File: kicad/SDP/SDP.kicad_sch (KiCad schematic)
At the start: 29 parts

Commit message: Added sheet
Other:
- added sheet GrinderSubsystem (grindersubsystem.kicad_sch)
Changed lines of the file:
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@@
     (pin "2")
-  )
-  (symbol (lib_id "power:+24V") (at 39.37 31.75 0) (unit 1)
-    (in_bom yes) (on_board yes) (fields_autoplaced)
-    (property "Reference" "#PWR?" (id 0) (at 39.37 35.56 0)
-      (effects (font (size 1.27 1.27)) hide)
-    )
-    (property "Value" "+24V" (id 1) (at 39.37 26.67 0))
-    (property "Footprint" "" (id 2) (at 39.37 31.75 0)
-      (effects (font (size 1.27 1.27)) hide)
-    )
-    (property "Datasheet" "" (id 3) (at 39.37 31.75 0)
-      (effects (font (size 1.27 1.27)) hide)
-    )
-    (pin "1")
   )
   (symbol (lib_id "Device:C") (at 666.75 21.59 0) (unit 1)
@@
     (pin "1")
   )
+  (symbol (lib_id "power:+12V") (at 39.37 33.02 0) (unit 1)
+    (in_bom yes) (on_board yes) (fields_autoplaced)
+    (property "Reference" "#PWR?" (id 0) (at 39.37 36.83 0)
+      (effects (font (size 1.27 1.27)) hide)
+    )
+    (property "Value" "+12V" (id 1) (at 39.37 27.94 0))
+    (property "Footprint" "" (id 2) (at 39.37 33.02 0)
+      (effects (font (size 1.27 1.27)) hide)
+    )
+    (property "Datasheet" "" (id 3) (at 39.37 33.02 0)
+      (effects (font (size 1.27 1.27)) hide)
+    )
+    (pin "1")
+  )
   (symbol (lib_name "GND_2") (lib_id "power:GND") (at 226.06 223.52 0) (unit 1)
     (in_bom yes) (on_board yes) (fields_autoplaced)
@@
     (pin "1")
   )
-  (sheet (at 326.39 33.02) (size 22.86 19.05) (fields_autoplaced)
+  (sheet (at 356.87 60.96) (size 20.32 19.05) (fields_autoplaced)
     (stroke (width 0.1524) (type solid) (color 0 0 0 0))
     (fill (color 0 0 0 0.0000))
-    (property "Sheet name" "FilterSubsystem" (id 0) (at 326.39 32.3084 0)
+    (property "Sheet name" "GrinderSubsystem" (id 0) (at 356.87 60.2484 0)
       (effects (font (size 1.27 1.27)) (justify left bottom))
     )
-    (property "Sheet file" "filtersubsystem.kicad_sch" (id 1) (at 326.39 52.6546 0)
+    (property "Sheet file" "grindersubsystem.kicad_sch" (id 1) (at 356.87 80.5946 0)
+      (effects (font (size 1.27 1.27)) (justify left top))
+    )
+  )
+  (sheet (at 356.87 31.75) (size 20.32 19.05) (fields_autoplaced)
+    (stroke (width 0.1524) (type solid) (color 0 0 0 0))
+    (fill (color 0 0 0 0.0000))
+    (property "Sheet name" "FilterSubsystem" (id 0) (at 356.87 31.0384 0)
+      (effects (font (size 1.27 1.27)) (justify left bottom))
+    )
+    (property "Sheet file" "filtersubsystem.kicad_sch" (id 1) (at 356.87 51.3846 0)
       (effects (font (size 1.27 1.27)) (justify left top))
     )
@@
     (path "/" (page "1"))
     (path "/a4a83c44-c8e0-453d-a09d-7474e32229cb" (page "2"))
+    (path "/60ab11df-7ec6-4862-a63f-21a5fb7314af" (page "3"))
   )
   (symbol_instances
@@
       (reference "#PWR?") (unit 1) (value "+3.3V") (footprint "")
     )
-    (path "/a4a83c44-c8e0-453d-a09d-7474e32229cb/101b1325-4279-4b67-96d2-6b5c97b1c400"
-      (reference "#PWR?") (unit 1) (value "+24V") (footprint "")
-    )
     (path "/13d8bfa6-d7d2-43b6-8fd6-aa77f4d342d5"
       (reference "#PWR?") (unit 1) (value "GND") (footprint "")
-    )
-    (path "/1be3e15d-4b9c-4cb1-b64b-2e6c6e28a3d9"
-      (reference "#PWR?") (unit 1) (value "+24V") (footprint "")
     )
     (path "/a4a83c44-c8e0-453d-a09d-7474e32229cb/22bb47d2-cad7-4e6f-9d0c-9f1abf96059d"
@@
       (reference "#PWR?") (unit 1) (value "GND") (footprint "")
     )
+    (path "/a4a83c44-c8e0-453d-a09d-7474e32229cb/c3b10306-ffea-4360-a540-14b7f64a3a06"
+      (reference "#PWR?") (unit 1) (value "+12V") (footprint "")
+    )
     (path "/c7457898-24d2-471b-adfd-6c8f1092010b"
       (reference "#PWR?") (unit 1) (value "+3.3VA") (footprint "")
@@
       (reference "#PWR?") (unit 1) (value "+3.3V") (footprint "")
     )
+    (path "/e3807980-a1cd-416c-873b-dd543df8b2fd"
+      (reference "#PWR?") (unit 1) (value "+12V") (footprint "")
+    )
     (path "/e4860a43-b5c8-40dc-8cba-8d3d99207cb6"

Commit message: Updated schematics
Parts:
- removed J?: Conn_01x06, symbol Connector_Generic:Conn_01x06
- added J?: RJ25, symbol Connector:RJ25
- added R?: 50k, symbol Device:R_Small
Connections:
- net +3V3: now also J?.2, R?.2
- net GND: now also J?.3
- net P13_MCLR: now also J?.1, R?.1
- net P26_PGC: now also J?.5
- net P27_PGD: now also J?.4
- net P6_GRD_RLY: now reaches U?.6 (T2CK/RC1)
- net P7_HTR_RLY: now reaches U?.7 (T3CK/RC2)
- no-connect marks 59 -> 60
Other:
- added sheet WaterSubsystem (watersubsystem.kicad_sch)

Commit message: Updated schematics
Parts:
- removed C? (x6): 0.1uF, symbol Device:C
- removed C?: 10uF, symbol Device:C
- removed U?: PIC24FJ128GA010-I_PT, TQFP100_12x12MC_MCH, symbol SDP-rescue:PIC24FJ128GA010-I_PT-2021-11-26_22-35-22
- added J?: Conn_01x04, symbol Connector_Generic:Conn_01x04
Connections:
- net +3V3: now also J?.3 (Pin_3)
- net GND: now also J?.4 (Pin_4)
- net P56_SDA1: now reaches U?.56 (SDA1/RG3)
- net P56_SDA1: now also J?.2 (Pin_2)
- net P57_SCL1: now reaches U?.57 (SCL1/RG2)
- net P57_SCL1: now also J?.1 (Pin_1)
- net P58_SCL2: now reaches U?.58 (SCL2/RA2)
- net P76_EN: now reaches U?.76 (OC2/RD1)
- net P77_STEP: now reaches U?.77 (OC3/RD2)
- net P78_DIR: now reaches U?.78 (PMBE/OC4/RD3)
- net P79_EN: now reaches U?.79 (IC5/RD12)
- net P80_STEP: now reaches U?.80 (CN19/RD13)
- net P81_DIR: now reaches U?.81 (PMWR/OC5/CN13/RD4)
- net P82_EN: now reaches U?.82 (PMRD/CN14/RD5)
- net P83_STEP: now reaches U?.83 (CN15/RD6)
- net P84_DIR: now reaches U?.84 (CN16/RD7)
- net P87_MTR1: now reaches U?.87 (RF0)
- net P88_MTR2: now reaches U?.88 (RF1)
- net P91_TEMP: now reaches U?.91 (RA6)
- net P95_TOF1_CE: now reaches U?.95 (RG14)
- net P96_TOF2_CE: now reaches U?.96 (RG12)
- net P97_TOF3_CE: now reaches U?.97 (RG13)
- net P59_!EN renamed P59_SDA2
- net P89_STEP: no longer names the net of U?.89 (RG1)
- net P90_DIR: no longer names the net of U?.90 (RG0)
- no-connect marks 60 -> 1
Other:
- added sheet BrewingSubsystem (brewingsubsystem.kicad_sch)
- note added: "LCD"
- note removed: "Bluetooth UART"
- note removed: "I2C Pins"
- note removed: "MPN: PIC24FJ128GA010-I_TP"

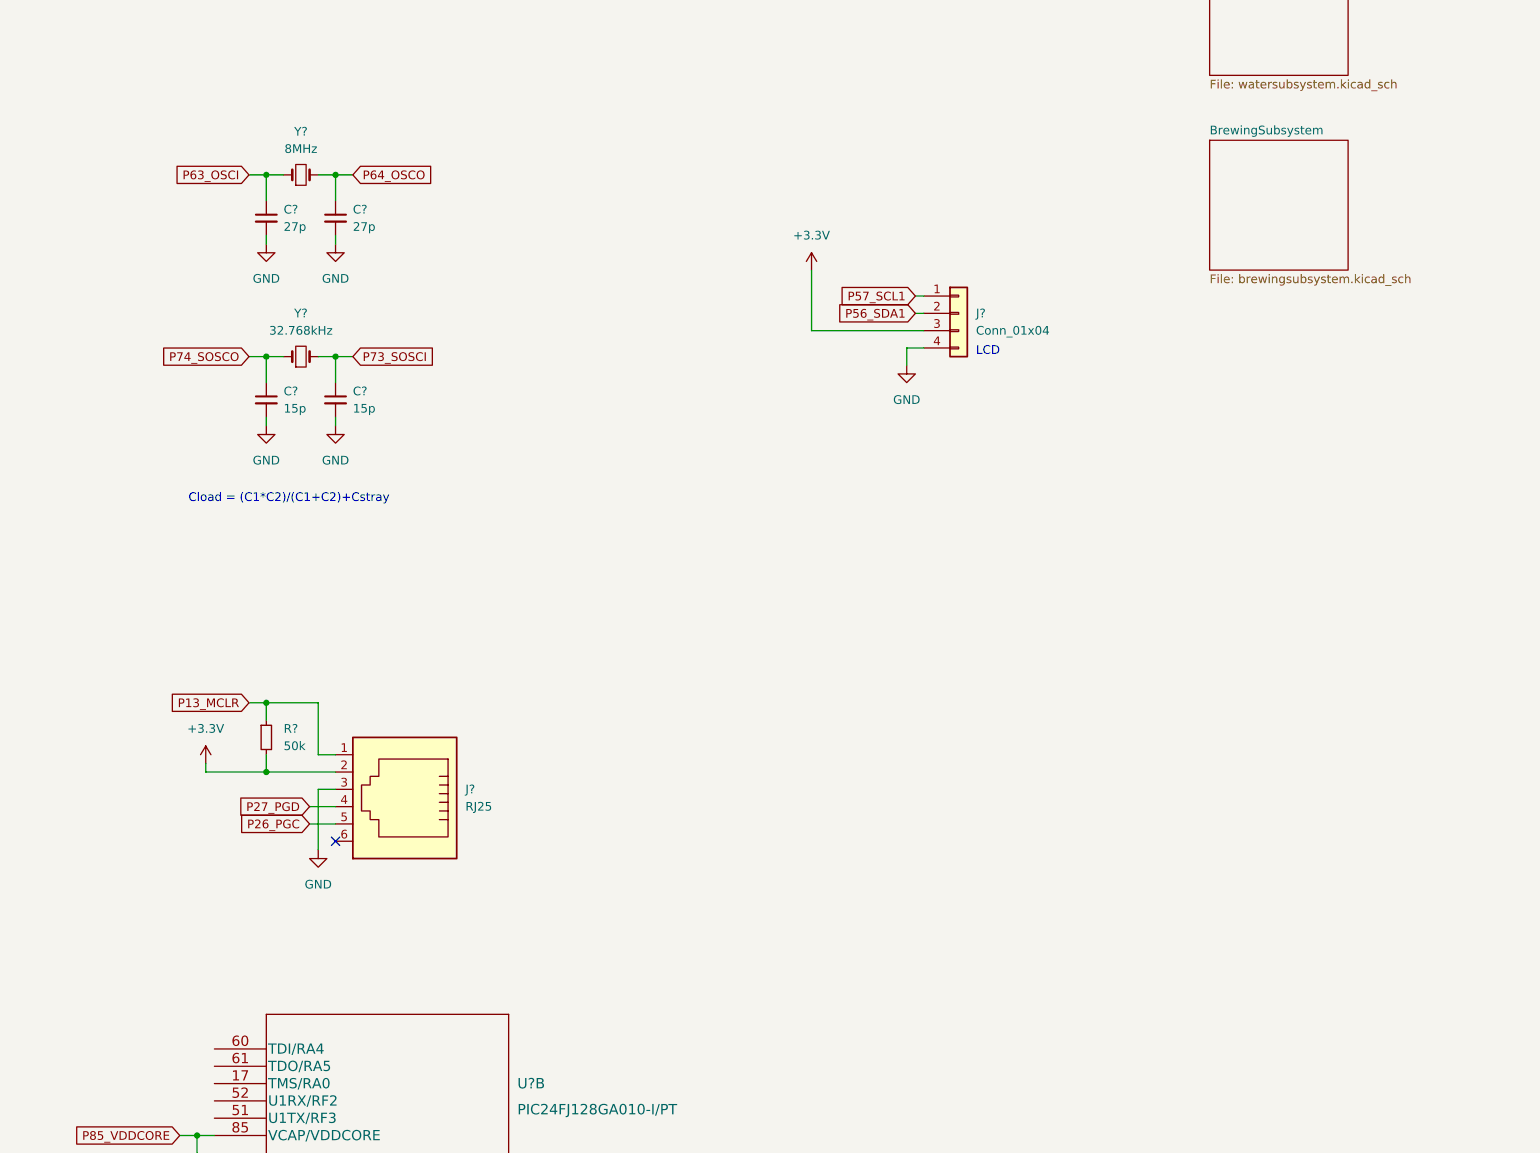
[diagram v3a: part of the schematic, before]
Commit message: Added DS3231 RTC and HM-10 BLE module
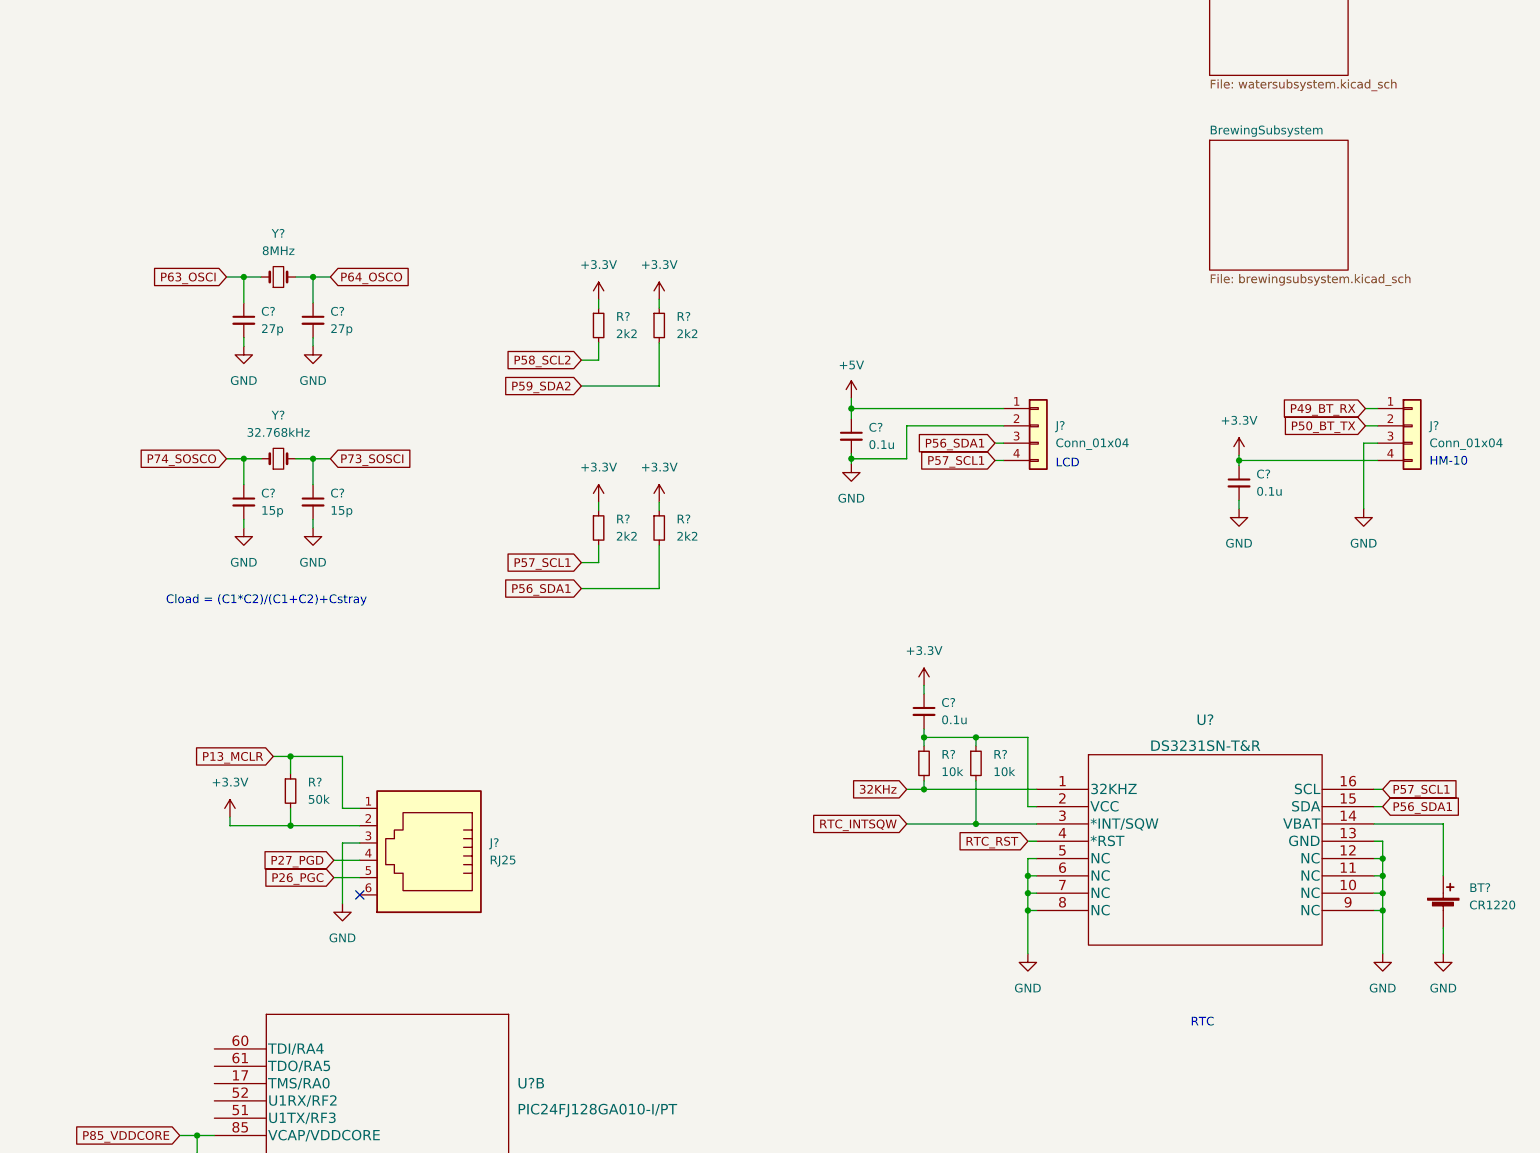
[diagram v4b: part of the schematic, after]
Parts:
- added BT?: CR1220, symbol Device:Battery_Cell
- added C? (x3): 0.1u, symbol Device:C_Small
- added J?: Conn_01x04, symbol Connector_Generic:Conn_01x04
- added R? (x2): 10k, symbol Device:R_Small
- added R? (x4): 2k2, symbol Device:R_Small
- added U?: DS3231SN-T&R, 21-0042B_16_MXM, symbol 2022-02-03_02-37-37:DS3231SN-T&R
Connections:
- net +3V3: now also C?.1, C?.1, J?.4 (Pin_4), R?.1, R?.1, R?.1, R?.1; no longer J?.3 (Pin_3)
- net +5V: now also J?.1 (Pin_1), C?.1
- net GND: now also J?.2 (Pin_2), BT?.2 (-), C?.2, C?.2, J?.3 (Pin_3), U?.10 (NC), U?.11 (NC), U?.12 (NC), U?.13 (GND), U?.5 (NC), U?.6 (NC), U?.7 (NC), U?.8 (NC), U?.9 (NC); no longer J?.4 (Pin_4)
- net P49_BT_RX: now also J?.1 (Pin_1)
- net P50_BT_TX: now also J?.2 (Pin_2)
- net P56_SDA1: now also J?.3 (Pin_3), R?.2, U?.15 (SDA); no longer J?.2 (Pin_2)
- net P57_SCL1: now also J?.4 (Pin_4), R?.2, U?.16 (SCL); no longer J?.1 (Pin_1)
- net P58_SCL2: now also R?.2
- net P59_SDA2: now also R?.2
- new net: BT?.1 (+), U?.14 (VBAT)
- new net: C?.2, R?.1, R?.1, U?.2 (VCC)
- new net 32KHz: R?.2, U?.1 (32KHZ)
- new net RTC_INTSQW: R?.2, U?.3 (*INT/SQW)
- new net RTC_RST: U?.4 (*RST)
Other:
- note added: "HM-10"
- note added: "RTC"
- moved on the sheet: C?, J?, R?, Y?

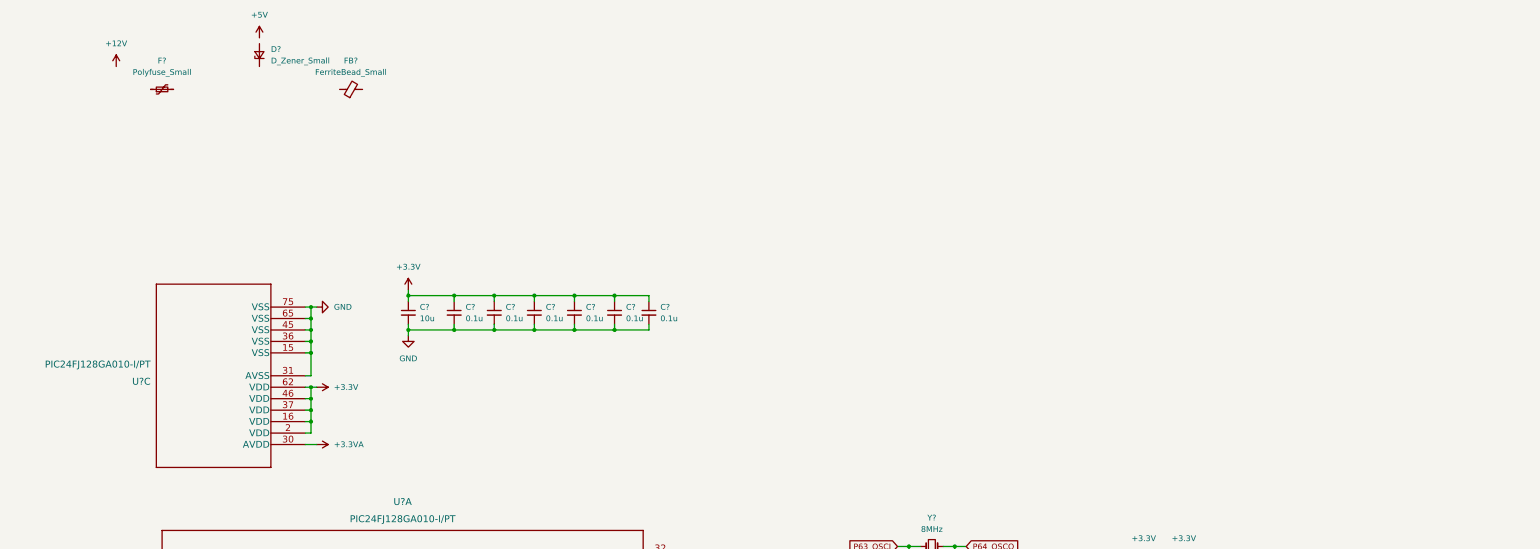
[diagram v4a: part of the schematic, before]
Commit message: Added 5V and 3.3V voltage regulators
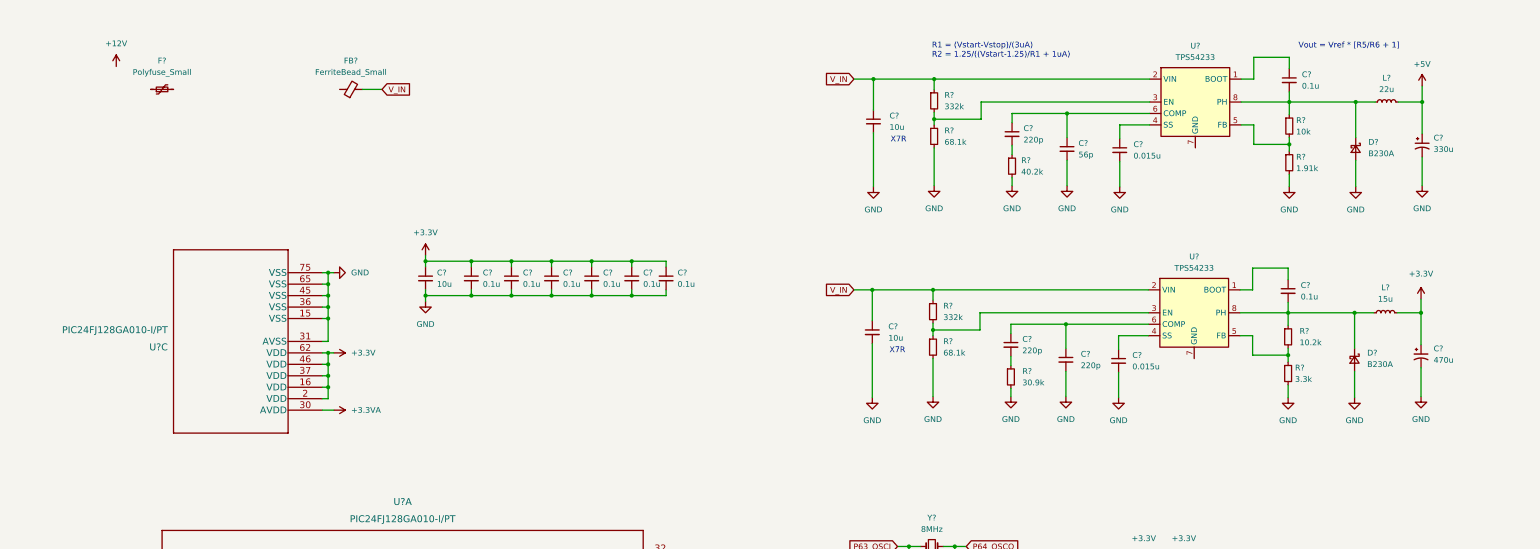
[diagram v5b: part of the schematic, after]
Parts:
- removed D?: D_Zener_Small, symbol Device:D_Zener_Small
- added C? (x3): 220p, symbol Device:C_Small
- added C? (x2): 10u, symbol Device:C_Small
- added C? (x2): 0.015u, symbol Device:C_Small
- added C?: 56p, symbol Device:C_Small
- added C?: 470u, symbol Device:C_Polarized_Small_US
- added C? (x2): 0.1u, symbol Device:C_Small
- added C?: 330u, symbol Device:C_Polarized_Small_US
- added D? (x2): B230A, symbol Device:D_Schottky_Small
- added L?: 22u, symbol Device:L_Small
- added L?: 15u, symbol Device:L_Small
- added R? (x2): 68.1k, symbol Device:R_Small
- added R?: 10.2k, symbol Device:R_Small
- added R?: 10k, symbol Device:R_Small
- added R?: 30.9k, symbol Device:R_Small
- added R? (x2): 332k, symbol Device:R_Small
- added R?: 1.91k, symbol Device:R_Small
- added R?: 3.3k, symbol Device:R_Small
- added R?: 40.2k, symbol Device:R_Small
- added U? (x2): TPS54233, Package_SO:SOIC-8_3.9x4.9mm_P1.27mm, symbol Regulator_Switching:TPS54233
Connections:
- net +3V3: now also C?.1, L?.2
- net +5V: now also C?.1, L?.2
- net GND: now also C?.2, C?.2, C?.2, C?.2, C?.2, C?.2, C?.2, C?.2, D?.2 (A), D?.2 (A), R?.2, R?.2, R?.2, R?.2, R?.2, R?.2
- net V_IN: now reaches FB?.2
- net V_IN: now also C?.1, C?.1, R?.1, R?.1, U?.2 (VIN), U?.2 (VIN)
- new net: C?.1, C?.1, U?.6 (COMP) (x2)
- new net: C?.1, U?.4 (SS) (x2)
- new net: R?.1, R?.2, U?.3 (EN) (x2)
- new net: C?.2, D?.1 (K), L?.1, R?.1, U?.8 (PH) (x2)
- new net: R?.1, R?.2, U?.5 (FB) (x2)
- new net: C?.2, R?.1 (x2)
- new net: C?.1, U?.1 (BOOT) (x2)
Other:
- note added: "R1 = (Vstart-Vstop)/(3uA) R2 = 1.25/((Vstart-1.25)/R1 + 1uA)"
- note added: "Vout = Vref * [R5/R6 + 1]"
- note added: "X7R"
- moved on the sheet: C?, U?C

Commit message: Updated power section
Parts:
- added D?: 12V, symbol Device:D_Zener_Small
- added MOSFET?: SSM3J334R_LFT, SOT-23F_TOS, symbol 2022-02-04_21-11-39:SSM3J334R_LFT
- F?: value Polyfuse_Small -> 2A
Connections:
- net +12V: now also F?.1
- net GND: now also D?.2 (A), MOSFET?.1 (GATE)
- net at F?.2: now also MOSFET?.3 (DRAIN)
- net at FB?.1: now also D?.1 (K), MOSFET?.2 (SOURCE)
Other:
- note added: "I2C Pullup"
- note added: "ISCP Programming Interface"
- note added: "PIC24 Microcontroller"
- note added: "Peripherals"
- note added: "Power"
- moved on the sheet: BT?, C?, FB?, J?, R?, U?, U?B
